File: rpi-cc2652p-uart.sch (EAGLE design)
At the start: 13 parts, among them U1 CC2652P2-DUOWEISI, U2 AP2112K

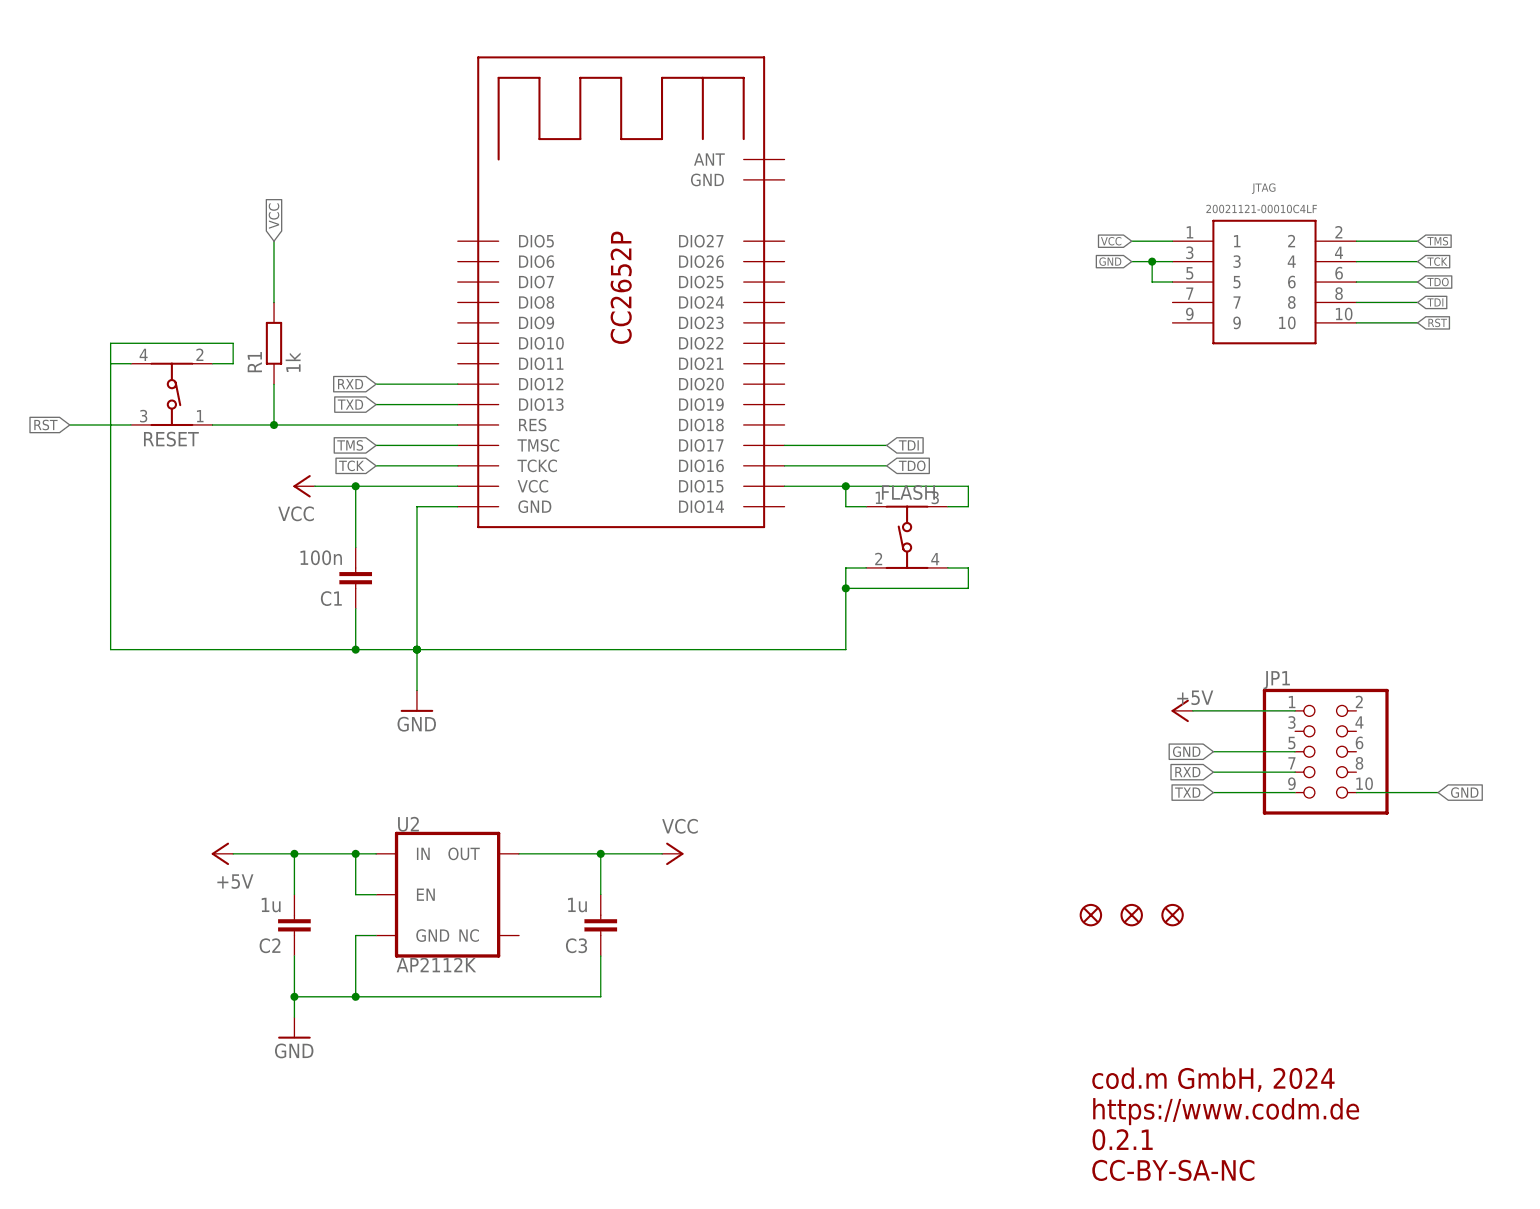
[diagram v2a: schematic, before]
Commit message: added CC LED on DIO7
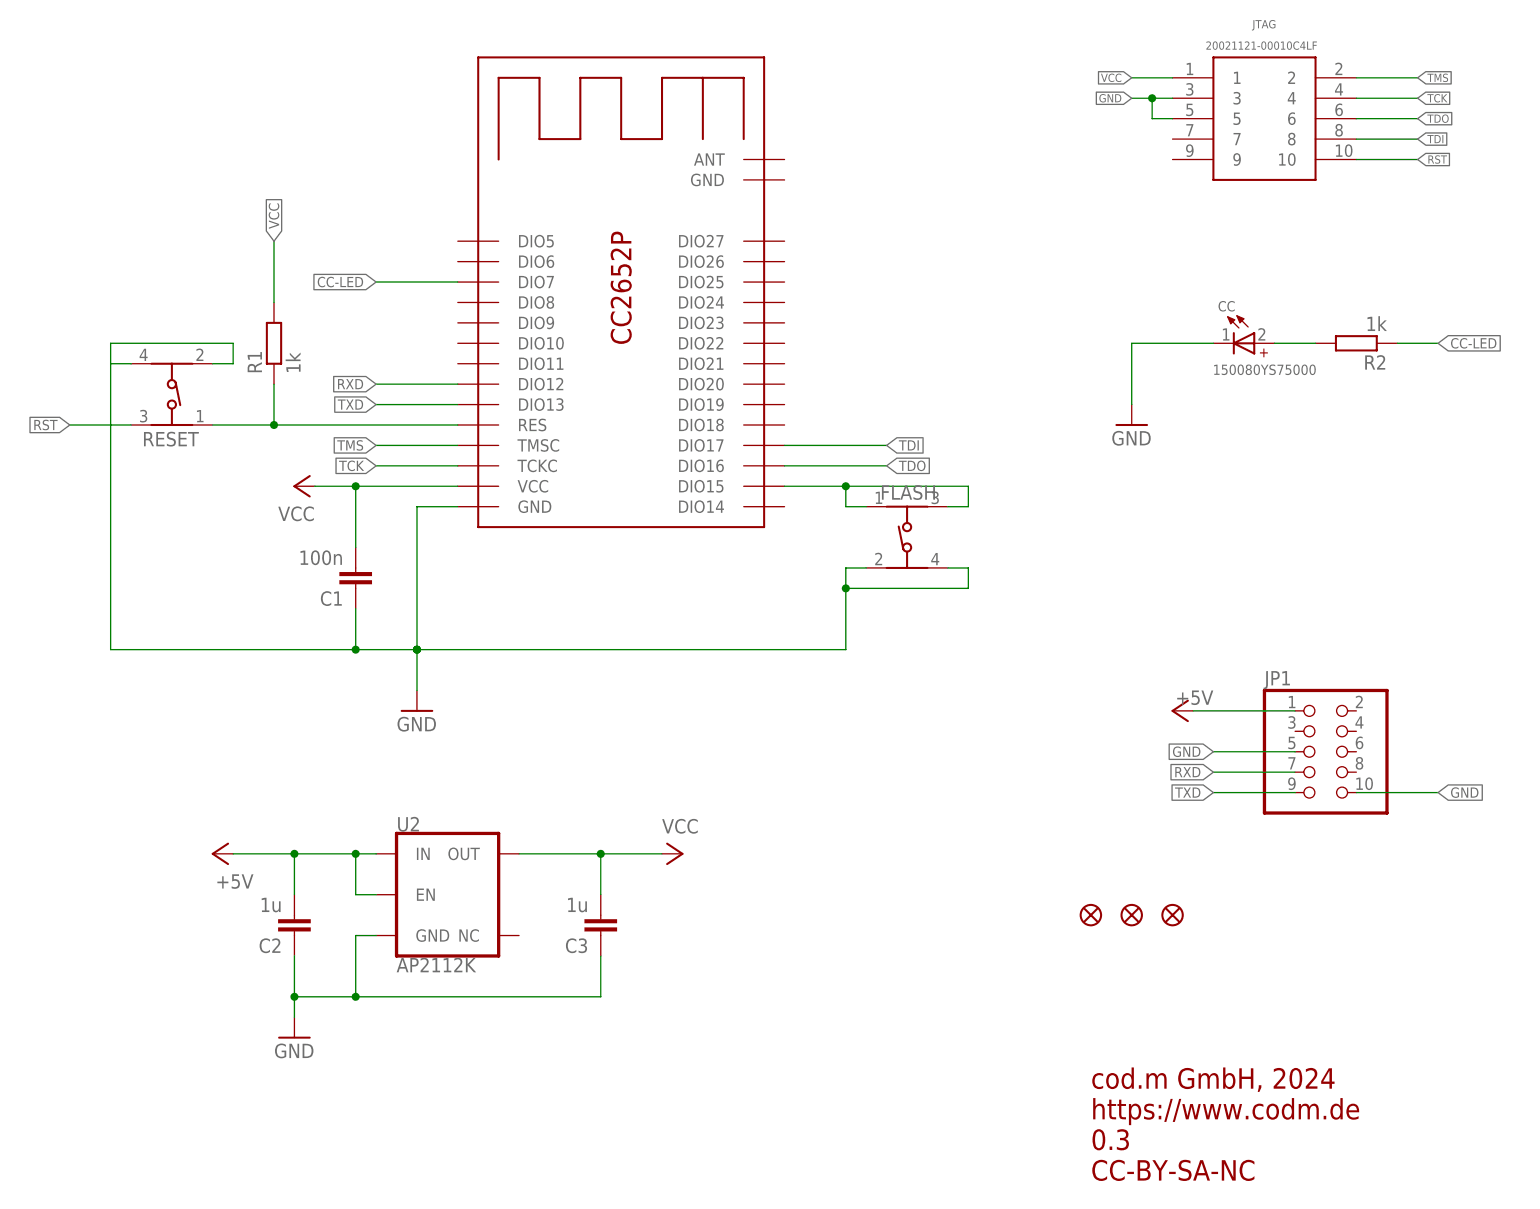
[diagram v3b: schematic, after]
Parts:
- added CC: 150080YS75000, Wurth_LEDs_WL-SMCW:WL-SMCW_0805_150080YS75000
- added R2: 1k, codm:R-EU_R0603RF
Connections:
- new net CC-LED: R2.1, U1.DIO7
- new net N$5: CC.+, R2.2
- net GND: now also CC.-
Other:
- note added: "cod.m GmbH, 2024 https://www.codm.de 0.3 CC-BY-SA-NC"
- note removed: "cod.m GmbH, 2024 https://www.codm.de 0.2.1 CC-BY-SA-NC"
- moved on the sheet: JTAG
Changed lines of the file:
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@@
 <part name="FD2" library="SparkFun-Aesthetics" library_urn="urn:adsk.eagle:library:507" deviceset="FIDUCIAL" device="1X2" package3d_urn="urn:adsk.eagle:package:41384560/3"/>
 <part name="FD3" library="SparkFun-Aesthetics" library_urn="urn:adsk.eagle:library:507" deviceset="FIDUCIAL" device="1X2" package3d_urn="urn:adsk.eagle:package:41384560/3"/>
+<part name="CC" library="Wurth_LEDs_WL-SMCW" library_urn="urn:adsk.eagle:library:19028156" deviceset="WL-SMCW_0805" device="" package3d_urn="urn:adsk.eagle:package:19028167/5" technology="_150080YS75000" value="150080YS75000"/>
+<part name="GND2" library="supply1" library_urn="urn:adsk.eagle:library:371" deviceset="GND" device=""/>
+<part name="R2" library="codm" library_urn="urn:adsk.eagle:library:11602856" deviceset="R-EU_" device="R0603RF" package3d_urn="urn:adsk.eagle:package:11602922/5" value="1k"/>
 </parts>
 <sheets>
@@
 <text x="185.42" y="-5.08" size="2.54" layer="94">cod.m GmbH, 2024
 https://www.codm.de
-0.2.1
+0.3
 CC-BY-SA-NC</text>
 </plain>
@@
 <attribute name="VALUE" x="87.122" y="95.25" size="1.778" layer="96" rot="R90"/>
 </instance>
-<instance part="JTAG" gate="G$1" x="195.58" y="111.76" smashed="yes">
-<attribute name="NAME" x="208.48" y="117.918" size="1.016" layer="95" align="bottom-right"/>
-<attribute name="VALUE" x="213.61" y="115.26" size="1.016" layer="96" align="bottom-right"/>
+<instance part="JTAG" gate="G$1" x="195.58" y="132.08" smashed="yes">
+<attribute name="NAME" x="208.48" y="138.238" size="1.016" layer="95" align="bottom-right"/>
+<attribute name="VALUE" x="213.61" y="135.58" size="1.016" layer="96" align="bottom-right"/>
 </instance>
 <instance part="RESET" gate="G$1" x="71.12" y="93.98" smashed="yes" rot="R180">
@@
 <instance part="FD2" gate="G$1" x="190.5" y="27.94" smashed="yes"/>
 <instance part="FD3" gate="G$1" x="195.58" y="27.94" smashed="yes"/>
+<instance part="CC" gate="G$1" x="203.2" y="99.06" smashed="yes">
+<attribute name="NAME" x="201.212" y="103.032" size="1.27" layer="95"/>
+<attribute name="VALUE" x="200.572" y="95.132" size="1.27" layer="96"/>
+</instance>
+<instance part="GND2" gate="1" x="190.5" y="88.9" smashed="yes">
+<attribute name="VALUE" x="187.96" y="86.36" size="1.778" layer="96"/>
+</instance>
+<instance part="R2" gate="G$1" x="218.44" y="99.06" smashed="yes" rot="R180">
+<attribute name="NAME" x="222.25" y="97.5614" size="1.778" layer="95" rot="R180"/>
+<attribute name="VALUE" x="222.25" y="102.362" size="1.778" layer="96" rot="R180"/>
+</instance>
 </instances>
 <busses>
@@
 <segment>
 <pinref part="JTAG" gate="G$1" pin="1"/>
-<wire x1="195.58" y1="111.76" x2="190.5" y2="111.76" width="0.1524" layer="91"/>
-<label x="190.5" y="111.76" size="1.016" layer="95" rot="R180" xref="yes"/>
+<wire x1="195.58" y1="132.08" x2="190.5" y2="132.08" width="0.1524" layer="91"/>
+<label x="190.5" y="132.08" size="1.016" layer="95" rot="R180" xref="yes"/>
 </segment>
 <segment>
@@
 <segment>
 <pinref part="JTAG" gate="G$1" pin="3"/>
-<wire x1="195.58" y1="109.22" x2="193.04" y2="109.22" width="0.1524" layer="91"/>
+<wire x1="195.58" y1="129.54" x2="193.04" y2="129.54" width="0.1524" layer="91"/>
 <pinref part="JTAG" gate="G$1" pin="5"/>
-<wire x1="193.04" y1="109.22" x2="190.5" y2="109.22" width="0.1524" layer="91"/>
-<wire x1="195.58" y1="106.68" x2="193.04" y2="106.68" width="0.1524" layer="91"/>
-<wire x1="193.04" y1="106.68" x2="193.04" y2="109.22" width="0.1524" layer="91"/>
-<junction x="193.04" y="109.22"/>
-<label x="190.5" y="109.22" size="1.016" layer="95" rot="R180" xref="yes"/>
+<wire x1="193.04" y1="129.54" x2="190.5" y2="129.54" width="0.1524" layer="91"/>
+<wire x1="195.58" y1="127" x2="193.04" y2="127" width="0.1524" layer="91"/>
+<wire x1="193.04" y1="127" x2="193.04" y2="129.54" width="0.1524" layer="91"/>
+<junction x="193.04" y="129.54"/>
+<label x="190.5" y="129.54" size="1.016" layer="95" rot="R180" xref="yes"/>
 </segment>
 <segment>
@@
 <pinref part="U2" gate="G$1" pin="GND"/>
 </segment>
+<segment>
+<pinref part="GND2" gate="1" pin="GND"/>
+<wire x1="190.5" y1="91.44" x2="190.5" y2="99.06" width="0.1524" layer="91"/>
+<pinref part="CC" gate="G$1" pin="-"/>
+<wire x1="200.66" y1="99.06" x2="190.5" y2="99.06" width="0.1524" layer="91"/>
+</segment>
 </net>
 <net name="RXD" class="0">
@@
 <segment>
 <pinref part="JTAG" gate="G$1" pin="10"/>
-<wire x1="218.44" y1="101.6" x2="226.06" y2="101.6" width="0.1524" layer="91"/>
-<label x="226.06" y="101.6" size="1.016" layer="95" xref="yes"/>
+<wire x1="218.44" y1="121.92" x2="226.06" y2="121.92" width="0.1524" layer="91"/>
+<label x="226.06" y="121.92" size="1.016" layer="95" xref="yes"/>
 </segment>
 <segment>
@@
 <segment>
 <pinref part="JTAG" gate="G$1" pin="2"/>
-<wire x1="218.44" y1="111.76" x2="226.06" y2="111.76" width="0.1524" layer="91"/>
-<label x="226.06" y="111.76" size="1.016" layer="95" xref="yes"/>
+<wire x1="218.44" y1="132.08" x2="226.06" y2="132.08" width="0.1524" layer="91"/>
+<label x="226.06" y="132.08" size="1.016" layer="95" xref="yes"/>
 </segment>
 </net>
@@
 <segment>
 <pinref part="JTAG" gate="G$1" pin="4"/>
-<wire x1="218.44" y1="109.22" x2="226.06" y2="109.22" width="0.1524" layer="91"/>
-<label x="226.06" y="109.22" size="1.016" layer="95" xref="yes"/>
+<wire x1="218.44" y1="129.54" x2="226.06" y2="129.54" width="0.1524" layer="91"/>
+<label x="226.06" y="129.54" size="1.016" layer="95" xref="yes"/>
 </segment>
 </net>
@@
 <segment>
 <pinref part="JTAG" gate="G$1" pin="6"/>
-<wire x1="218.44" y1="106.68" x2="226.06" y2="106.68" width="0.1524" layer="91"/>
-<label x="226.06" y="106.68" size="1.016" layer="95" xref="yes"/>
+<wire x1="218.44" y1="127" x2="226.06" y2="127" width="0.1524" layer="91"/>
+<label x="226.06" y="127" size="1.016" layer="95" xref="yes"/>
 </segment>
 </net>
@@
 <segment>
 <pinref part="JTAG" gate="G$1" pin="8"/>
-<wire x1="218.44" y1="104.14" x2="226.06" y2="104.14" width="0.1524" layer="91"/>
-<label x="226.06" y="104.14" size="1.016" layer="95" xref="yes"/>
+<wire x1="218.44" y1="124.46" x2="226.06" y2="124.46" width="0.1524" layer="91"/>
+<label x="226.06" y="124.46" size="1.016" layer="95" xref="yes"/>
 </segment>
 </net>
@@
 </segment>
 </net>
+<net name="N$5" class="0">
+<segment>
+<pinref part="CC" gate="G$1" pin="+"/>
+<wire x1="208.28" y1="99.06" x2="213.36" y2="99.06" width="0.1524" layer="91"/>
+<pinref part="R2" gate="G$1" pin="2"/>
+</segment>
+</net>
+<net name="CC-LED" class="0">
+<segment>
+<pinref part="U1" gate="G$1" pin="DIO7"/>
+<wire x1="106.68" y1="106.68" x2="96.52" y2="106.68" width="0.1524" layer="91"/>
+<label x="96.52" y="106.68" size="1.27" layer="95" rot="R180" xref="yes"/>
+</segment>
+<segment>
+<wire x1="223.52" y1="99.06" x2="228.6" y2="99.06" width="0.1524" layer="91"/>
+<label x="228.6" y="99.06" size="1.27" layer="95" xref="yes"/>
+<pinref part="R2" gate="G$1" pin="1"/>
+</segment>
+</net>
